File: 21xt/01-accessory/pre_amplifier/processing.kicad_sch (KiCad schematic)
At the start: 6 parts, among them IC2 AD5679RBCPZ-1

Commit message: completed schemtic
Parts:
- added IC21, IC22: MAX7301AAI+, SOP65P778X199-28N, symbol 21xt_preamp-symbols:MAX7301AAI+
- added R81, R82: 120k, symbol Device:R
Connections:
- net GND: now also IC21.2 (GND_1), IC21.3 (GND_2), IC22.2 (GND_1), IC22.3 (GND_2), R81.1, R82.1
- net MISO: now also IC21.4 (DOUT), IC22.4 (DOUT)
- net MOSI: now also IC21.26 (DIN), IC22.26 (DIN)
- new net: IC22.1 (ISET), R82.2
- new net: IC21.1 (ISET), R81.2
- new net 5V: IC21.28 (V+), IC22.28 (V+)
- new net CS_amp: IC21.27 (~{CS})
- new net CS_sg: IC22.27 (~{CS})
- new net P12: IC21.5 (P12)
- new net P12_2: IC22.5 (P12)
- new net P13: IC21.6 (P13)
- new net P13_2: IC22.6 (P13)
- new net P14: IC21.7 (P14)
- new net P14_2: IC22.7 (P14)
- new net P15: IC21.8 (P15)
- new net P15_2: IC22.8 (P15)
- new net P16: IC21.9 (P16)
- new net P16_2: IC22.9 (P16)
- new net P17: IC21.10 (P17)
- new net P17_2: IC22.10 (P17)
- new net P18: IC21.11 (P18)
- new net P18_2: IC22.11 (P18)
- new net P19: IC21.12 (P19)
- new net P19_2: IC22.12 (P19)
- new net P20: IC21.13 (P20)
- new net P20_2: IC22.13 (P20)
- new net P21: IC21.14 (P21)
- new net P21_2: IC22.14 (P21)
- new net P22_2: IC22.15 (P22)
- new net P23_2: IC22.16 (P23)
- new net P24_2: IC22.17 (P24)
- new net P25_2: IC22.18 (P25)
- new net P26_2: IC22.19 (P26)
- new net P27_2: IC22.20 (P27)
- new net P28_2: IC22.21 (P28)
- new net P29_2: IC22.22 (P29)
- new net P30_2: IC22.23 (P30)
- new net P31_2: IC22.24 (P31)
- new net SLCK: IC21.25 (SCLK), IC22.25 (SCLK)
- no-connect marks 6 -> 16
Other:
- note added: "DAC: 1) refulator 2) 'output to accessory' connector"
- note added: "Don't need to level shift down the expander"
- note added: "expander IC21: 1) switches for in-amps 2)'output to accessory' connector"
- note added: "expander IC22: 1) switches for strain gauges 2) 'output to accessory' connector"

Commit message: Reviewed schematic
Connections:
- net 5v_reful is gone; now on net 5v_buck: C10.2, C11.2, C8.2, C9.2, IC2.18 (VLOGIC), IC2.2 (VDD), IC2.6 (GAIN)
- net 5V renamed 5v_buck
- net GND renamed GNDD
- net GNDD: no longer C10.1, C11.1, C12.1, C8.1, C9.1, IC2.29 (EP)
- new net GNDA: C10.1, C11.1, C12.1, C8.1, C9.1, IC2.29 (EP)
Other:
- note added: "DAC: 1) buck converter 2) 'output to accessory' connector"
- note removed: "DAC: 1) refulator 2) 'output to accessory' connector"

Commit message: added footprints
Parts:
- IC21, IC22: footprint SOP65P778X199-28N -> pre_amp_footprint_lib:MAX7301AAI_footprint
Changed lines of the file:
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@@
 			)
 		)
-		(property "Footprint" "SOP65P778X199-28N"
+		(property "Footprint" "pre_amp_footprint_lib:MAX7301AAI_footprint"
 			(at 246.38 183.82 0)
 			(effects
@@
 			)
 		)
-		(property "Footprint" "SOP65P778X199-28N"
+		(property "Footprint" "pre_amp_footprint_lib:MAX7301AAI_footprint"
 			(at 186.69 183.82 0)
 			(effects

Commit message: added footprints
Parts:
- IC21, IC22: footprint pre_amp_footprint_lib:MAX7301AAI_footprint -> 21xt_footprints:SOP65P777X199-28N
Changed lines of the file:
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@@
 			)
 		)
-		(property "Footprint" "pre_amp_footprint_lib:MAX7301AAI_footprint"
+		(property "Footprint" "21xt_footprints:SOP65P777X199-28N"
 			(at 246.38 183.82 0)
 			(effects
@@
 			)
 		)
-		(property "Footprint" "pre_amp_footprint_lib:MAX7301AAI_footprint"
+		(property "Footprint" "21xt_footprints:SOP65P777X199-28N"
 			(at 186.69 183.82 0)
 			(effects

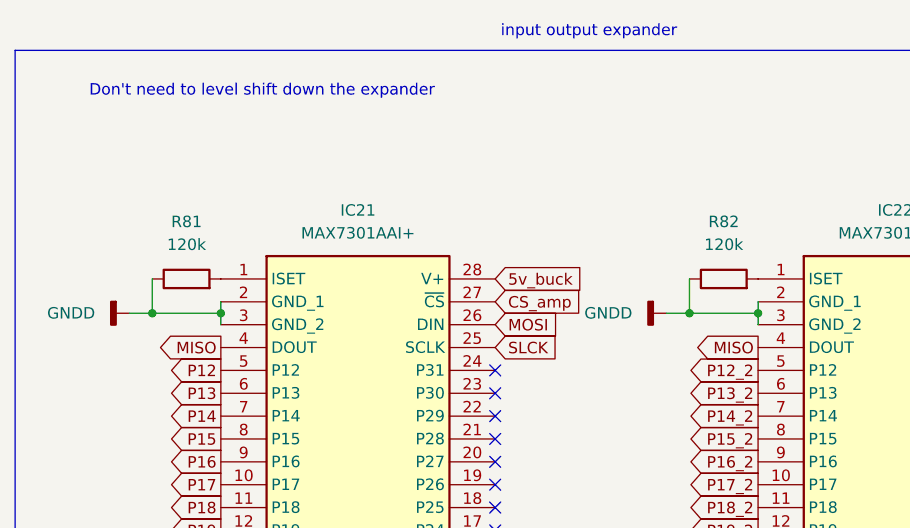
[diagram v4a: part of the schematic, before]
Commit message: assigned footprints
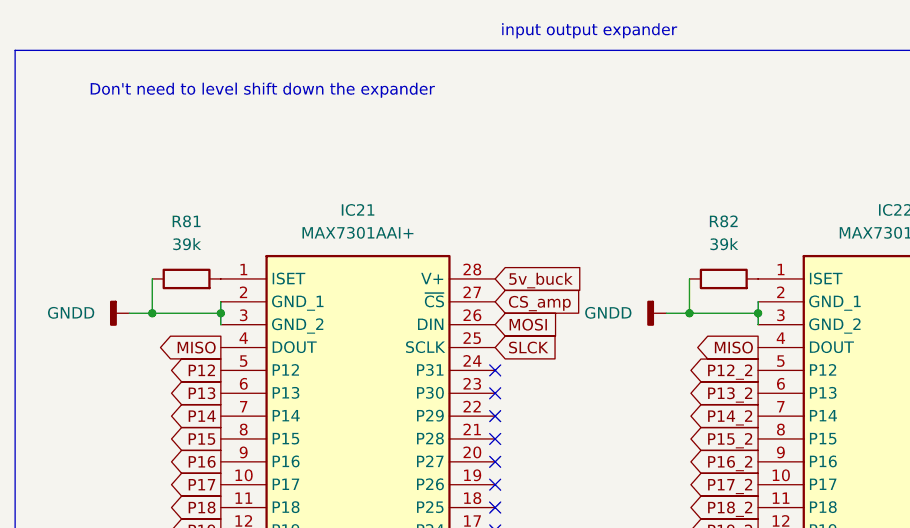
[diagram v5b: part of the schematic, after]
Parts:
- C10, C12, C8: footprint (none) -> Capacitor_SMD:C_0402_1005Metric
- C11, C9: footprint (none) -> Capacitor_SMD:C_0603_1608Metric
- R81, R82: value 120k -> 39k; footprint (none) -> Resistor_SMD:R_0603_1608Metric
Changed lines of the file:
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@@
 			)
 		)
-		(property "Footprint" ""
+		(property "Footprint" "Capacitor_SMD:C_0603_1608Metric"
 			(at 38.4048 100.33 0)
 			(effects
@@
 			)
 		)
-		(property "Footprint" ""
+		(property "Footprint" "Capacitor_SMD:C_0402_1005Metric"
 			(at 93.6752 97.79 0)
 			(effects
@@
 			)
 		)
-		(property "Footprint" ""
+		(property "Footprint" "Capacitor_SMD:C_0603_1608Metric"
 			(at 115.8748 105.41 0)
 			(effects
@@
 			)
 		)
-		(property "Value" "120k"
+		(property "Value" "39k"
 			(at 156.21 85.09 90)
 			(effects
@@
 			)
 		)
-		(property "Footprint" ""
+		(property "Footprint" "Resistor_SMD:R_0603_1608Metric"
 			(at 156.21 90.678 90)
 			(effects
@@
 			)
 		)
-		(property "Footprint" ""
+		(property "Footprint" "Capacitor_SMD:C_0402_1005Metric"
 			(at 32.0548 100.33 0)
 			(effects
@@
 			)
 		)
-		(property "Value" "120k"
+		(property "Value" "39k"
 			(at 215.9 85.09 90)
 			(effects
@@
 			)
 		)
-		(property "Footprint" ""
+		(property "Footprint" "Resistor_SMD:R_0603_1608Metric"
 			(at 215.9 90.678 90)
 			(effects
@@
 			)
 		)
-		(property "Footprint" ""
+		(property "Footprint" "Capacitor_SMD:C_0402_1005Metric"
 			(at 109.5248 105.41 0)
 			(effects
